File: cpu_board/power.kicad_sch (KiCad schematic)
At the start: 45 parts, among them U1 TPS16630PWPR, U10 CD40109BQNSRQ1, U7 TPS54226PWPRPWP14_2P31X2P46-L, U8 TPS54226PWPRPWP14_2P31X2P46-L, U9 LT3014IS5-TRMPBF

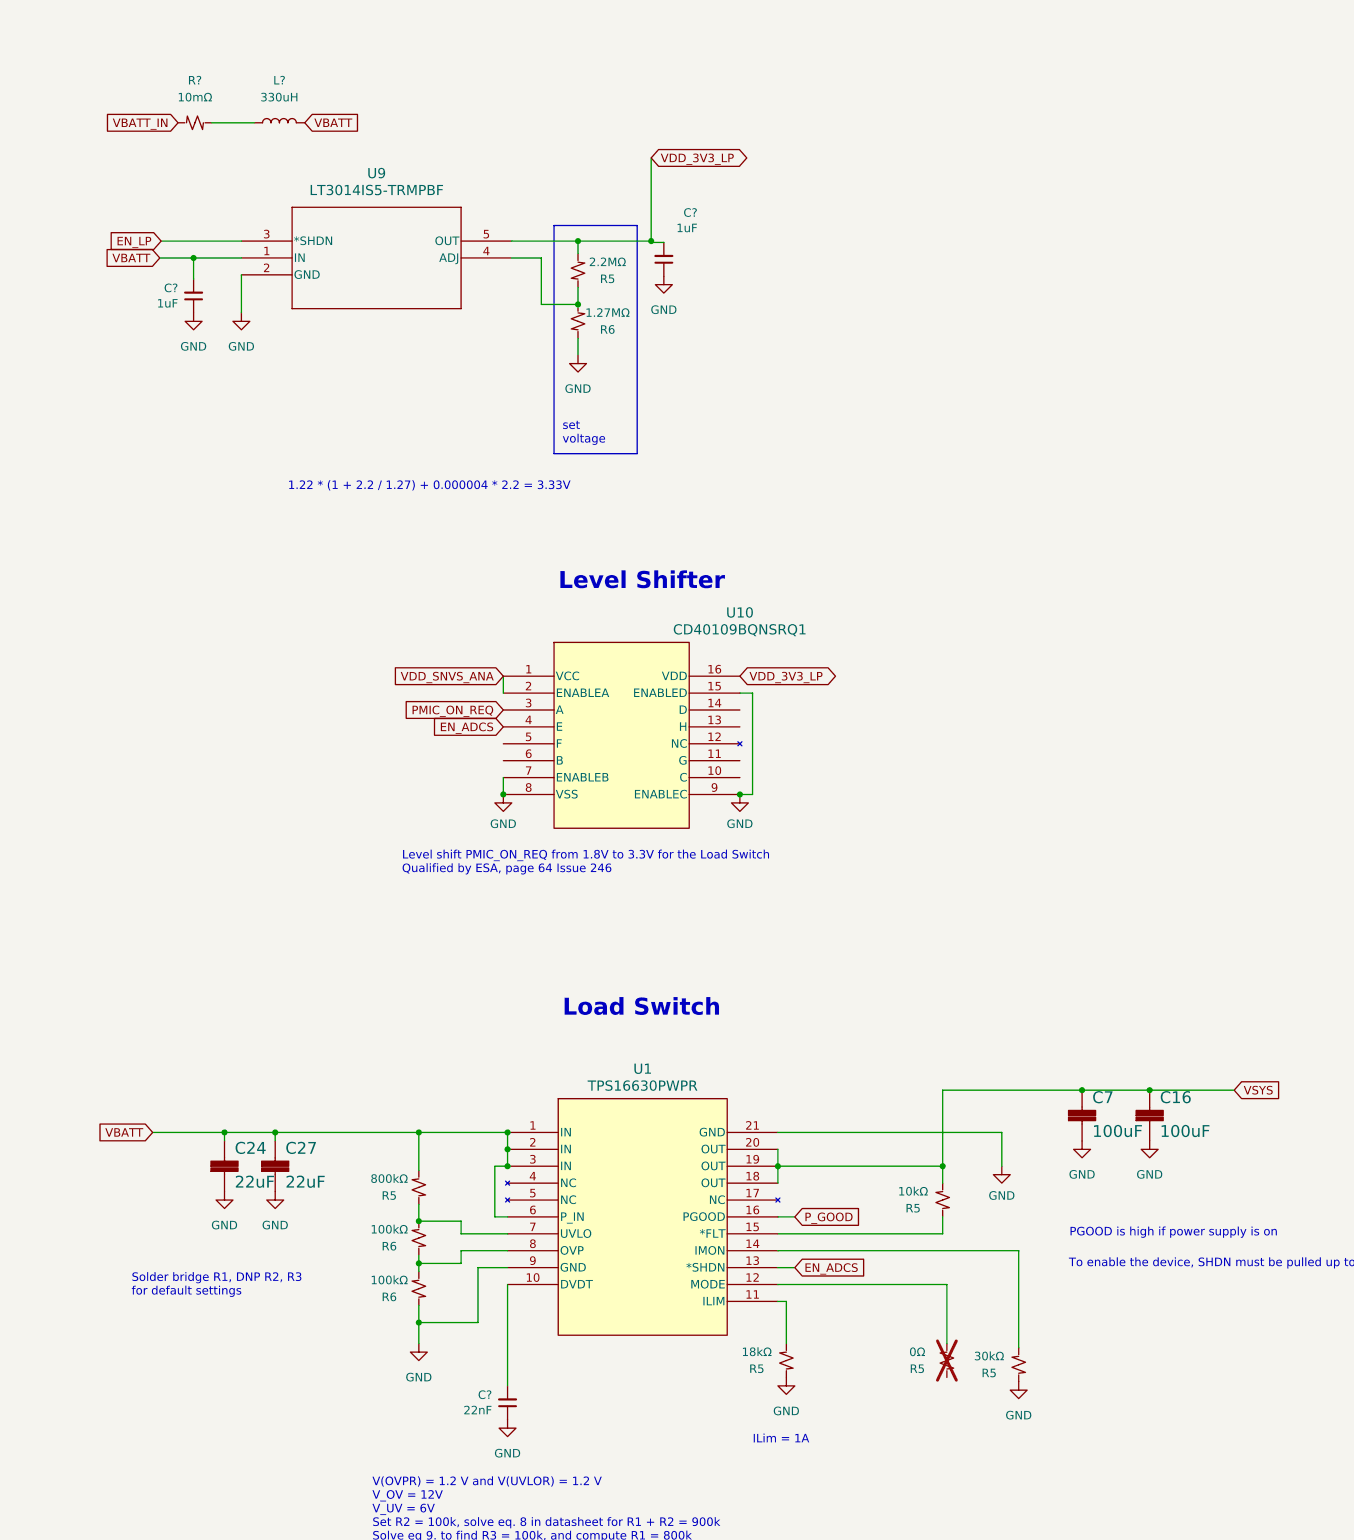
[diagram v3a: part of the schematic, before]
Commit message: move level shifter to top
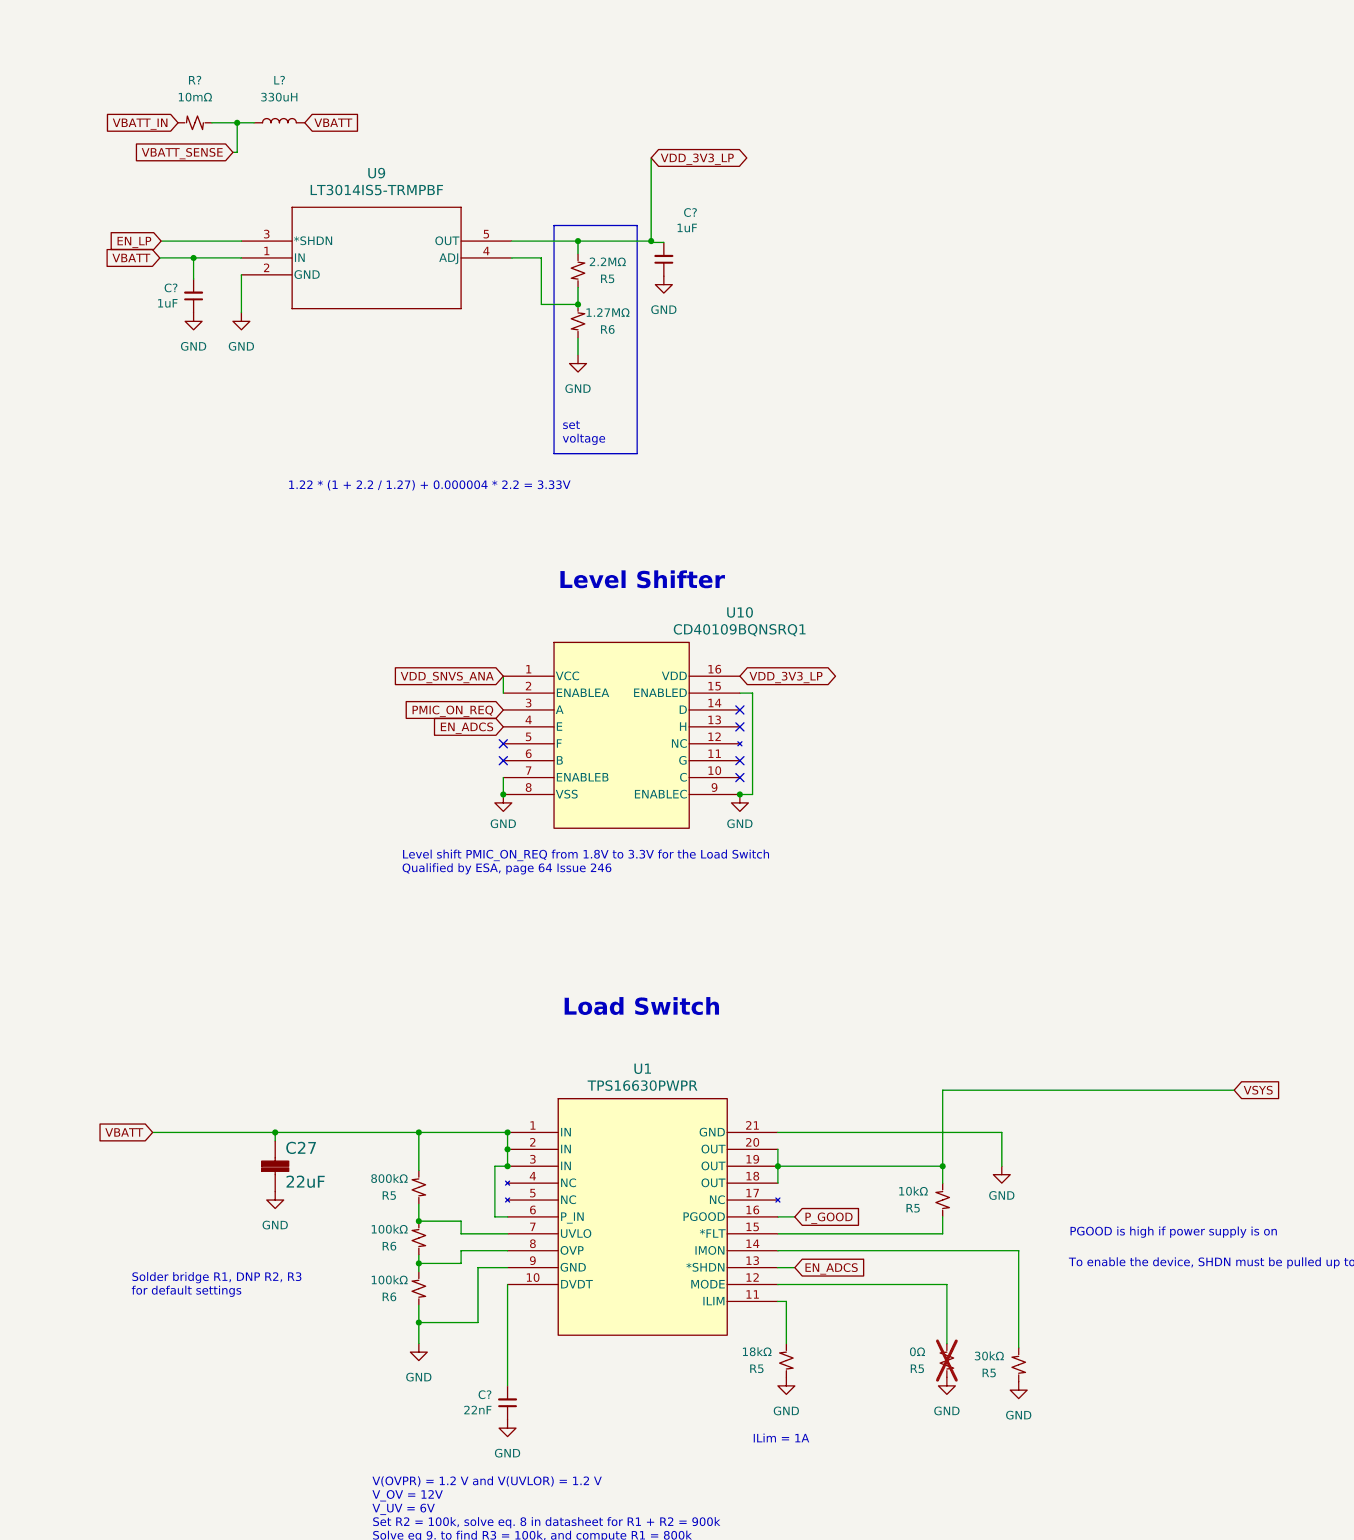
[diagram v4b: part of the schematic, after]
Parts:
- removed C16, C7: 100uF, adcs:Perfect_0402, symbol mainboard:22UF-1210-16V-20%
- removed C24: 22uF, adcs:Perfect_0402, symbol mainboard:22UF-0805-6.3V-20%
- C27, C76, C77, C78, C80: footprint adcs:Perfect_0402 -> Capacitor_SMD:C_0603_1608Metric
- C79, C81, C82, C83: footprint adcs:Perfect_0402 -> Capacitor_SMD:C_1210_3225Metric
- U1: footprint HTSSOP20_PWP_TEX -> adcs:HTSSOP20_PWP_TEX
- U10: footprint NS16 -> adcs:NS16
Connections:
- net GND: now also R5.1
- net VBATT_SENSE: now reaches L?.1, R?.2
- no-connect marks 0 -> 6

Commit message: clean up silkscreen
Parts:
- C27, C76, C77, C78, C80: Footprint (for JLCPCB) 0402 -> 0603
- U1: Flight (none) -> TPS16630PWPR; JLCPCB P/N (none) -> C1849462
- U10: JLCPCB P/N (none) -> C2677390
- U9: JLCPCB P/N Proto C666277 -> (none)
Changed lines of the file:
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@@
       (effects (font (size 1.27 1.27)) hide)
     )
-    (property "Datasheet" "~" (at 67.945 50.8 0)
+    (property "Datasheet" "" (at 67.945 50.8 0)
       (effects (font (size 1.27 1.27)) hide)
     )
@@
       (effects (font (size 1.27 1.27)) hide)
     )
-    (property "Footprint (for JLCPCB)" "0402" (at 264.795 110.49 0)
+    (property "Footprint (for JLCPCB)" "0603" (at 264.795 110.49 0)
       (effects (font (size 1.27 1.27)) hide)
     )
@@
       (effects (font (size 1.27 1.27)) hide)
     )
-    (property "Footprint (for JLCPCB)" "0402" (at 67.31 208.915 0)
+    (property "Footprint (for JLCPCB)" "0603" (at 67.31 208.915 0)
       (effects (font (size 1.27 1.27)) hide)
     )
@@
     (property "Power Rating" "" (at 101.6 133.985 0)
       (effects (font (size 1.27 1.27)))
+    )
+    (property "Description" "Level Shifter" (at 101.6 133.985 0)
+      (effects (font (size 1.27 1.27)) hide)
+    )
+    (property "JLCPCB P/N" "C2677390" (at 101.6 133.985 0)
+      (effects (font (size 1.27 1.27)) hide)
     )
     (pin "1")
@@
     (property "Power Rating" "" (at 102.235 202.565 0)
       (effects (font (size 1.27 1.27)))
+    )
+    (property "Description" "Load Switch" (at 102.235 202.565 0)
+      (effects (font (size 1.27 1.27)) hide)
+    )
+    (property "Flight" "TPS16630PWPR" (at 102.235 202.565 0)
+      (effects (font (size 1.27 1.27)) hide)
+    )
+    (property "JLCPCB P/N" "C1849462" (at 102.235 202.565 0)
+      (effects (font (size 1.27 1.27)) hide)
     )
     (pin "1")
@@
       (effects (font (size 1.27 1.27)) hide)
     )
-    (property "Footprint (for JLCPCB)" "0402" (at 265.43 175.895 0)
+    (property "Footprint (for JLCPCB)" "0603" (at 265.43 175.895 0)
       (effects (font (size 1.27 1.27)) hide)
     )
@@
       (effects (font (size 1.27 1.27)) hide)
     )
-    (property "JLCPCB P/N Proto" "C666277" (at 62.23 68.58 0)
+    (property "JLCPCB P/N Proto" "" (at 62.23 68.58 0)
       (effects (font (size 1.27 1.27)) hide)
     )
@@
       (effects (font (size 1.27 1.27)) hide)
     )
-    (property "Footprint (for JLCPCB)" "0402" (at 272.415 110.49 0)
+    (property "Footprint (for JLCPCB)" "0603" (at 272.415 110.49 0)
       (effects (font (size 1.27 1.27)) hide)
     )
@@
       (effects (font (size 1.27 1.27)) hide)
     )
-    (property "Footprint (for JLCPCB)" "0402" (at 273.05 175.895 0)
-      (effects (font (size 1.27 1.27)) hide)
-    )
+    (property "Footprint (for JLCPCB)" "0603" (at 273.05 175.895 0)
+      (effects (font (size 1.27 1.27)) hide)
+    )

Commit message: soldermander 1.0 ready for review
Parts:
- C27, C76, C77, C78, C80: Voltage Rating (none) -> 6.3V
- C79, C81, C82, C83, C84, C85, C86, C87, C88, C89, C? (x3): Voltage Rating (none) -> 50V
- R27: JLCPCB P/N (none) -> C208856
- R5: value 800kΩ -> 806kΩ; JLCPCB P/N (none) -> C3016043
- R?: Footprint (for JLCPCB) 0402 -> 2512; JLCPCB P/N (none) -> C5116354; Power Rating (none) -> 3W
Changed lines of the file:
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@@
       (effects (font (size 1.27 1.27)))
+    )
+    (property "Voltage Rating" "50V" (at 292.735 120.65 0)
+      (effects (font (size 1.27 1.27)) hide)
     )
     (pin "1")
@@
       (effects (font (size 1.27 1.27)))
     )
+    (property "Voltage Rating" "50V" (at 384.81 201.295 0)
+      (effects (font (size 1.27 1.27)) hide)
+    )
     (pin "1")
     (pin "2")
@@
     (property "Power Rating" "" (at 55.0418 76.835 0)
       (effects (font (size 1.27 1.27)))
+    )
+    (property "Voltage Rating" "50V" (at 55.0418 76.835 0)
+      (effects (font (size 1.27 1.27)) hide)
     )
     (pin "1")
@@
       (effects (font (size 1.27 1.27)))
     )
+    (property "Voltage Rating" "50V" (at 125.73 71.3232 0)
+      (effects (font (size 1.27 1.27)) hide)
+    )
     (pin "1")
     (pin "2")
@@
       (effects (font (size 1.27 1.27)) hide)
     )
+    (property "Voltage Rating" "50V" (at 283.21 193.675 0)
+      (effects (font (size 1.27 1.27)) hide)
+    )
     (pin "1")
     (pin "2")
@@
       (effects (font (size 1.27 1.27)) hide)
     )
-    (property "JLCPCB P/N" "" (at 363.855 133.35 0)
+    (property "JLCPCB P/N" "C208856" (at 363.855 133.35 0)
       (effects (font (size 1.27 1.27)) hide)
     )
@@
       (effects (font (size 1.27 1.27)) hide)
     )
+    (property "Voltage Rating" "6.3V" (at 264.795 110.49 0)
+      (effects (font (size 1.27 1.27)) hide)
+    )
     (pin "1")
     (pin "2")
@@
       (effects (font (size 1.27 1.27)))
     )
-    (property "Value" "800kΩ" (at 84.455 209.55 0)
+    (property "Value" "806kΩ" (at 84.455 209.55 0)
       (effects (font (size 1.27 1.27)))
     )
@@
       (effects (font (size 1.27 1.27)) hide)
     )
-    (property "JLCPCB P/N" "" (at 88.9 210.82 0)
+    (property "JLCPCB P/N" "C3016043" (at 88.9 210.82 0)
       (effects (font (size 1.27 1.27)) hide)
     )
@@
       (effects (font (size 1.27 1.27)))
     )
+    (property "Voltage Rating" "50V" (at 377.19 186.055 0)
+      (effects (font (size 1.27 1.27)) hide)
+    )
     (pin "1")
     (pin "2")
@@
     (property "Power Rating" "" (at 102.235 243.205 0)
       (effects (font (size 1.27 1.27)))
+    )
+    (property "Voltage Rating" "50V" (at 102.235 243.205 0)
+      (effects (font (size 1.27 1.27)) hide)
     )
     (pin "1")
@@
       (effects (font (size 1.27 1.27)))
     )
+    (property "Voltage Rating" "50V" (at 384.175 135.89 0)
+      (effects (font (size 1.27 1.27)) hide)
+    )
     (pin "1")
     (pin "2")
@@
       (effects (font (size 1.27 1.27)) hide)
     )
+    (property "Voltage Rating" "6.3V" (at 67.31 208.915 0)
+      (effects (font (size 1.27 1.27)) hide)
+    )
     (pin "1")
     (pin "2")
@@
   )
   (symbol (lib_id "Device:R_Small_US") (at 55.245 50.8 90) (unit 1)
-    (in_bom yes) (on_board yes) (dnp no) (fields_autoplaced)
-    (property "Reference" "R?" (at 55.245 44.45 90)
-      (effects (font (size 1.27 1.27)))
-    )
-    (property "Value" "10mΩ" (at 55.245 46.99 90)
+    (in_bom yes) (on_board yes) (dnp no)
+    (property "Reference" "R?" (at 55.245 43.815 90)
+      (effects (font (size 1.27 1.27)))
+    )
+    (property "Value" "10mΩ" (at 55.245 45.72 90)
       (effects (font (size 1.27 1.27)))
     )
@@
       (effects (font (size 1.27 1.27)) hide)
     )
-    (property "JLCPCB P/N" "" (at 55.245 50.8 0)
+    (property "JLCPCB P/N" "C5116354" (at 55.245 50.8 0)
       (effects (font (size 1.27 1.27)) hide)
     )
@@
       (effects (font (size 1.27 1.27)) hide)
     )
-    (property "Footprint (for JLCPCB)" "0402" (at 55.245 50.8 0)
+    (property "Footprint (for JLCPCB)" "2512" (at 55.245 50.8 0)
       (effects (font (size 1.27 1.27)) hide)
     )
@@
       (effects (font (size 1.27 1.27)))
     )
-    (property "Power Rating" "" (at 55.245 50.8 0)
+    (property "Power Rating" "3W" (at 55.245 48.26 90)
       (effects (font (size 1.27 1.27)))
     )
@@
       (effects (font (size 1.27 1.27)))
     )
+    (property "Voltage Rating" "50V" (at 376.555 120.65 0)
+      (effects (font (size 1.27 1.27)) hide)
+    )
     (pin "1")
     (pin "2")
@@
     )
     (property "Footprint (for JLCPCB)" "1210" (at 282.575 128.27 0)
+      (effects (font (size 1.27 1.27)) hide)
+    )
+    (property "Voltage Rating" "50V" (at 282.575 128.27 0)
       (effects (font (size 1.27 1.27)) hide)
     )
@@
       (effects (font (size 1.27 1.27)) hide)
     )
+    (property "Voltage Rating" "6.3V" (at 265.43 175.895 0)
+      (effects (font (size 1.27 1.27)) hide)
+    )
     (pin "1")
     (pin "2")
@@
       (effects (font (size 1.27 1.27)) hide)
     )
+    (property "Voltage Rating" "6.3V" (at 272.415 110.49 0)
+      (effects (font (size 1.27 1.27)) hide)
+    )
     (pin "1")
     (pin "2")
@@
       (effects (font (size 1.27 1.27)) hide)
     )
+    (property "Voltage Rating" "6.3V" (at 273.05 175.895 0)
+      (effects (font (size 1.27 1.27)) hide)
+    )
     (pin "1")
     (pin "2")
@@
       (effects (font (size 1.27 1.27)) hide)
     )
+    (property "Voltage Rating" "50V" (at 273.05 193.675 0)
+      (effects (font (size 1.27 1.27)) hide)
+    )
     (pin "1")
     (pin "2")
@@
     (property "Power Rating" "" (at 293.37 186.055 0)
       (effects (font (size 1.27 1.27)))
+    )
+    (property "Voltage Rating" "50V" (at 293.37 186.055 0)
+      (effects (font (size 1.27 1.27)) hide)
     )
     (pin "1")
@@
       (effects (font (size 1.27 1.27)) hide)
     )
+    (property "Voltage Rating" "50V" (at 272.415 128.27 0)
+      (effects (font (size 1.27 1.27)) hide)
+    )

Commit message: update
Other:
- company: (none) -> Stanford Student Space Initiative
- title: (none) -> Soldermander
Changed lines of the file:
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@@
 (kicad_sch (version 20230121) (generator eeschema)
   (paper "A3")
+  (title_block
+    (title "Soldermander")
+    (date "2024-02-27")
+    (rev "1.0")
+    (company "Stanford Student Space Initiative")
+    (comment 1 "RE: Flynn Dreilinger")
+  )
   (junction (at 88.9 222.25) (diameter 0) (color 0 0 0 0)
   )
